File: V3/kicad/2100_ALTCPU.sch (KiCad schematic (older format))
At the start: 8 parts, among them U2100 Z8-L180-S180-180-PQFP-80, U2101 GAL16V8, X2100 14.7456 MHz

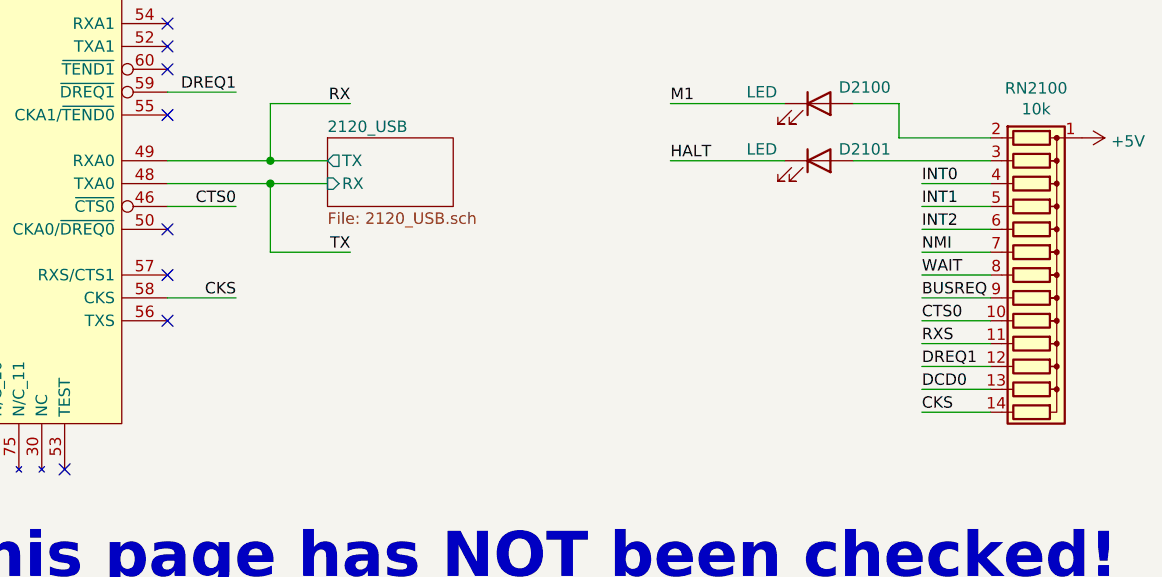
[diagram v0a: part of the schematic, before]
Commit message: routed memory and some control signals
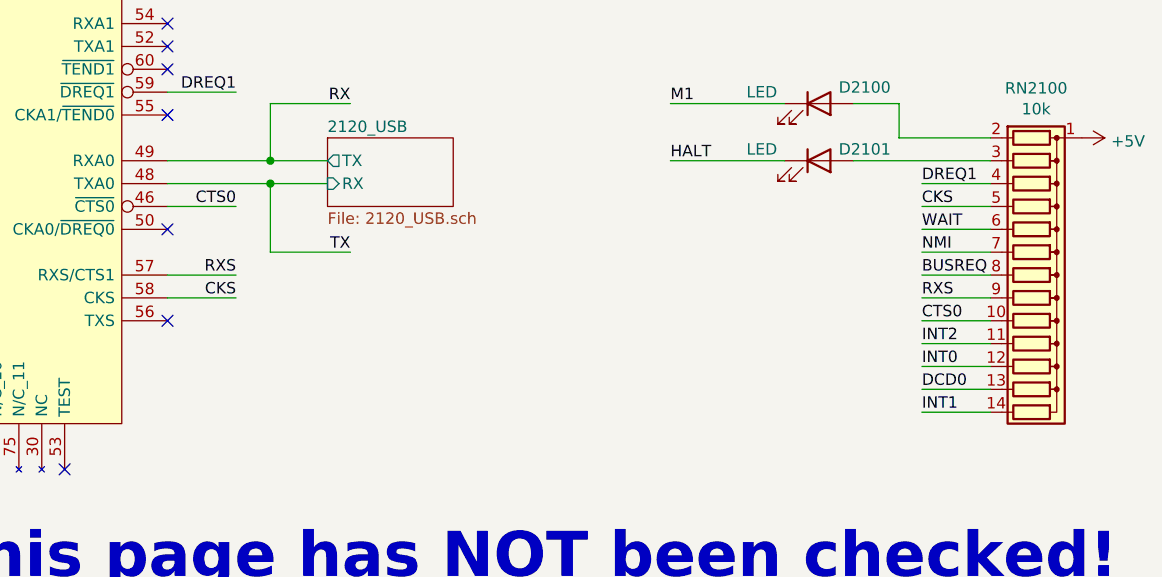
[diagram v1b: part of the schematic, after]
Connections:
- net BUSREQ: now also RN2100.8 (R7); no longer RN2100.9 (R8)
- net CKS: now also RN2100.5 (R4); no longer RN2100.14 (R13)
- net DREQ1: now also RN2100.4 (R3); no longer RN2100.12 (R11)
- net INT: now also RN2100.12 (R11); no longer RN2100.4 (R3)
- net INT1: now also RN2100.14 (R13); no longer RN2100.5 (R4)
- net INT2: now also RN2100.11 (R10); no longer RN2100.6 (R5)
- net RXS: now also RN2100.9 (R8), U2100.57 (RXS/CTS1); no longer RN2100.11 (R10)
- net WAIT: now also RN2100.6 (R5); no longer RN2100.8 (R7)
- no-connect marks 13 -> 12
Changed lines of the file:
@@
 INT1
 Wire Wire Line
-	10350 4700 10050 4700
-Wire Wire Line
-	10350 4600 10050 4600
-Text Label 10050 4700 0    50   ~ 0
+	10350 5200 10050 5200
+Wire Wire Line
+	10350 5500 10050 5500
+Text Label 10050 5200 0    50   ~ 0
 INT2
-Text Label 10050 4600 0    50   ~ 0
+Text Label 10050 5500 0    50   ~ 0
 INT1
 Wire Wire Line
@@
 WAIT
 Wire Wire Line
-	10350 5000 10050 5000
-Text Label 10050 5000 0    50   ~ 0
-BUSREQ
-Wire Wire Line
 	10350 4900 10050 4900
 Text Label 10050 4900 0    50   ~ 0
+BUSREQ
+Wire Wire Line
+	10350 4700 10050 4700
+Text Label 10050 4700 0    50   ~ 0
 WAIT
 Wire Wire Line
@@
 CTS0
 Wire Wire Line
-	10350 5300 10050 5300
-Text Label 10050 5300 0    50   ~ 0
+	10350 4500 10050 4500
+Text Label 10050 4500 0    50   ~ 0
 DREQ1
 Wire Wire Line
@@
 M1
 Wire Wire Line
-	10350 4500 10050 4500
-Text Label 10050 4500 0    50   ~ 0
+	10350 5300 10050 5300
+Text Label 10050 5300 0    50   ~ 0
 INT0
 Wire Wire Line
@@
 NoConn ~ 6750 4700
 Wire Wire Line
-	10350 5200 10050 5200
-Text Label 10050 5200 0    50   ~ 0
+	10350 5000 10050 5000
+Text Label 10050 5000 0    50   ~ 0
 RXS
 Wire Wire Line
-	10350 5500 10050 5500
-Text Label 10050 5500 0    50   ~ 0
+	10350 4600 10050 4600
+Text Label 10050 4600 0    50   ~ 0
 CKS
-NoConn ~ 6750 4900
 Wire Wire Line
 	6750 5000 7050 5000
@@
 NoConn ~ 6750 3800
 NoConn ~ 6750 3900
+Wire Wire Line
+	6750 4900 7050 4900
+Text Label 7050 4900 2    50   ~ 0
+RXS
 Wire Bus Line
 	4300 3550 4300 4250

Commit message: Final checks and DRC
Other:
- note added: "This page has been checked!"
- note removed: "This page has NOT been checked!"
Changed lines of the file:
@@
 Text Label 3700 4650 0    50   ~ 0
 CLK
-Text Notes 5750 6250 0    197  ~ 39
-This page has NOT been checked!
+Text Notes 7700 6950 0    118  ~ 24
+This page has been checked!
 Text Label 7050 2500 2    50   ~ 0
 MREQ

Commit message: Reworking 3.0 board
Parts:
- U2100: footprint Package_QFP:PQFP-80_14x20mm_P0.8mm -> Z180-Custom-Footprint:PQFP-80_14x20mm_P0.8mm
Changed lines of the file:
@@
 F 0 "U2100" H 4800 1350 50  0000 R TNN
 F 1 "Z8-L180-S180-180-PQFP-80" V 4310 450 50  0001 C CNN
-F 2 "Package_QFP:PQFP-80_14x20mm_P0.8mm" H 4850 2150 50  0001 L CNN
+F 2 "Z180-Custom-Footprint:PQFP-80_14x20mm_P0.8mm" H 4850 2150 50  0001 L CNN
 F 3 "http://www.zilog.com/docs/z180/z8s180ps.pdf" V 4700 1350 50  0001 L CNN
 F 4 "Microprocessors - MPU 20MHz STATIC Z180 XT" H 4850 2350 50  0001 L CNN "Description"

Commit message: on to autoroute
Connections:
- net C_RST: now also U2101.19 (IO1); no longer U2101.12 (IO8)
- net ROM_CS: now also U2101.12 (IO8); no longer U2101.19 (IO1)
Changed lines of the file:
@@
 Text Label 1750 6050 0    50   ~ 0
 IORQ
-Text HLabel 3000 5950 2    50   Output ~ 0
+Text HLabel 3000 6650 2    50   Output ~ 0
 ROM_CS
 Text Label 1750 6650 0    50   ~ 0
@@
 Text Label 4300 4550 0    50   ~ 0
 PHI
-Text Label 3300 6650 2    50   ~ 0
+Text Label 3300 5950 2    50   ~ 0
 C_RST
 Wire Wire Line
-	3000 6650 3300 6650
+	3000 5950 3300 5950
 Wire Wire Line
 	6750 2900 7050 2900

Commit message: Design Rule Check
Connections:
- net AUX_CS: no longer names the net of U2101.17 (I03)
- no-connect marks 12 -> 15
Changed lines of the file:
@@
 Text HLabel 7050 3100 2    50   Output ~ 0
 RD
-Text HLabel 7050 3200 2    50   Output ~ 0
-WR
 NoConn ~ 6750 4000
 NoConn ~ 4600 4750
@@
 Text HLabel 3000 6050 2    50   Output ~ 0
 H_RAM_CS
-Text HLabel 3000 6150 2    50   Output ~ 0
-AUX_CS
 Text HLabel 3000 6250 2    50   Output ~ 0
 PIO_EN
@@
 Text Label 7050 4900 2    50   ~ 0
 RXS
+NoConn ~ 3000 6550
+NoConn ~ 3000 6150
+NoConn ~ 7050 2900
 Wire Bus Line
 	4300 3550 4300 4250

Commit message: just totally redid the whole thing
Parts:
- removed D2101: LED, LED_THT:LED_D3.0mm, symbol Device:LED
- removed RN2100: 10k, Resistor_THT:R_Array_SIP14, symbol Device:R_Network13
- added D1: LED, LED_THT:LED_D3.0mm, symbol Device:LED
- added R1, R10, R11, R12, R13, R2, R3, R4, R5, R6, R7, R8, R9: R, Resistor_SMD:R_1206_3216Metric, symbol Device:R
- C2100, C2101: footprint Capacitor_THT:C_Rect_L4.0mm_W2.5mm_P2.50mm -> Capacitor_SMD:C_1206_3216Metric
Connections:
- net +5V: now also R1.1, R10.1, R11.1, R12.1, R13.1, R2.1, R3.1, R4.1, R5.1, R6.1, R7.1, R8.1, R9.1
- net A18: no longer U2101.7 (I7)
- net A19: now also U2101.6 (I6); no longer U2101.8 (I8)
- net A7: now also U2101.5 (I5); no longer U2101.6 (I6)
- net BUSREQ: now also R10.2
- net CKS: now also R7.2
- net CTS0: now also R12.2
- net DCD0: now also R4.2
- net DREQ1: now also R6.2
- net HALT: now also D1.1 (K)
- net INT: now also R3.2
- net INT1: now also R5.2
- net INT2: now also R13.2
- net MREAD: now also U2101.16 (IO4); no longer U2101.15 (IO5)
- net MWRITE: now also U2101.15 (IO5); no longer U2101.14 (IO6)
- net NMI: now also R9.2
- net PIO_EN: now also U2101.17 (I03); no longer U2101.16 (IO4)
- net ROM_CS: now also U2101.14 (IO6); no longer U2101.12 (IO8)
- net RTS0: no longer U2101.5 (I5)
- net RXS: now also R11.2
- net WAIT: now also R8.2
- net at D2100.2 (A): now also R1.2
- new net: D1.2 (A), R2.2
- no-connect marks 15 -> 13
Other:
- moved on the sheet: C2100, C2101, D2100

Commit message: More rearranging
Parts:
- added D2102/ST1, D2103/RTS1: LED, LED_THT:LED_D3.0mm, symbol Device:LED
- added R16, R17: R, Resistor_SMD:R_1206_3216Metric, symbol Device:R
- U2100: footprint Z180-Custom-Footprint:PQFP-80_14x20mm_P0.8mm -> UL_Z180:Z8018008FSG
- renumbered D2100 to D2100/M1, D1 to D2101/H1
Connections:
- net MREAD is gone; now on net ROM_CS: U2101.16 (IO4)
- net +5V: no longer R1.1, R2.1
- net A19: now also U2101.5 (I5); no longer U2101.6 (I6)
- net A7: now also U2101.4 (I4); no longer U2101.5 (I5)
- net CLK: now also U2101.1 (I1/CLK)
- net GND: now also R1.1, R2.1, U2101.11 (I10/~OE~), R16.1, R17.1
- net HALT: now also D2101/H1.2 (A); no longer D2101/H1.1 (K)
- net IORQ: now also U2101.3 (I3); no longer U2101.2 (I2)
- net M1: now also D2100/M1.2 (A); no longer D2100/M1.1 (K)
- net MREQ: now also U2101.2 (I2); no longer U2101.1 (I1/CLK)
- net RD: no longer U2101.3 (I3)
- net ROM_CS: no longer U2101.14 (IO6)
- net RTS0: now also D2103/RTS1.2 (A)
- net WR: no longer U2101.4 (I4)
- net ST: now reaches U2100.7 (ST)
- net ST: now also D2102/ST1.2 (A)
- net at R1.2: now also D2100/M1.1 (K); no longer D2100/M1.2 (A)
- net at R2.2: now also D2101/H1.1 (K); no longer D2101/H1.2 (A)
- net BUSACK: no longer names the net of U2100.78 (~BUSACK)
- net H_RAM_CS renamed RAM_CS
- net MWRITE: no longer names the net of U2101.15 (IO5)
- new net: D2102/ST1.1 (K), R16.2
- new net: D2103/RTS1.1 (K), R17.2
- no-connect marks 13 -> 14
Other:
- note removed: "RTS0 defaults to 1 and can be controlled via internal registers\nSetting it low disables part of the ROM window"
- moved on the sheet: D2100/M1, D2101/H1, R10, R11, R12, R13, R3, R4, R5, R6, R7, R8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
